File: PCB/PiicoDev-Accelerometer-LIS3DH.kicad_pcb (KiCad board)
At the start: 2 copper layers, 25.4 x 25.4 mm, 37 parts, among them J1 , J2 , J3 Conn_PiicoDev_header_01x04_Ma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, J4 INT, SW1 ASW, U1 LIS3DH

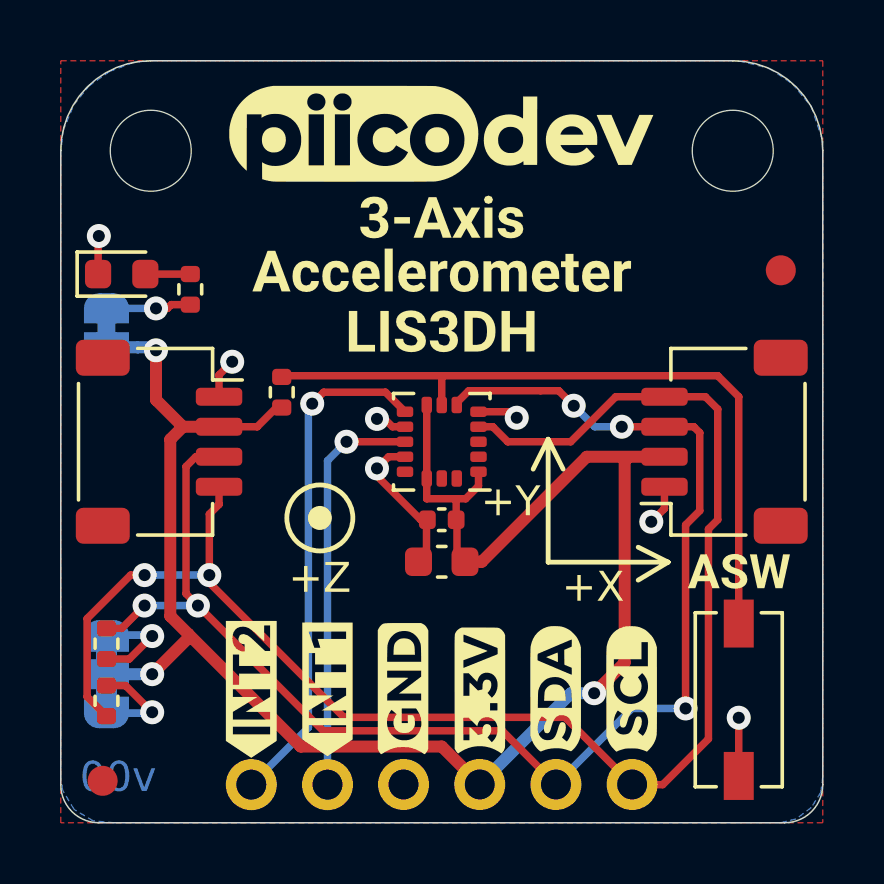
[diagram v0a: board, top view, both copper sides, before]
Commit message: add documents and link CAD
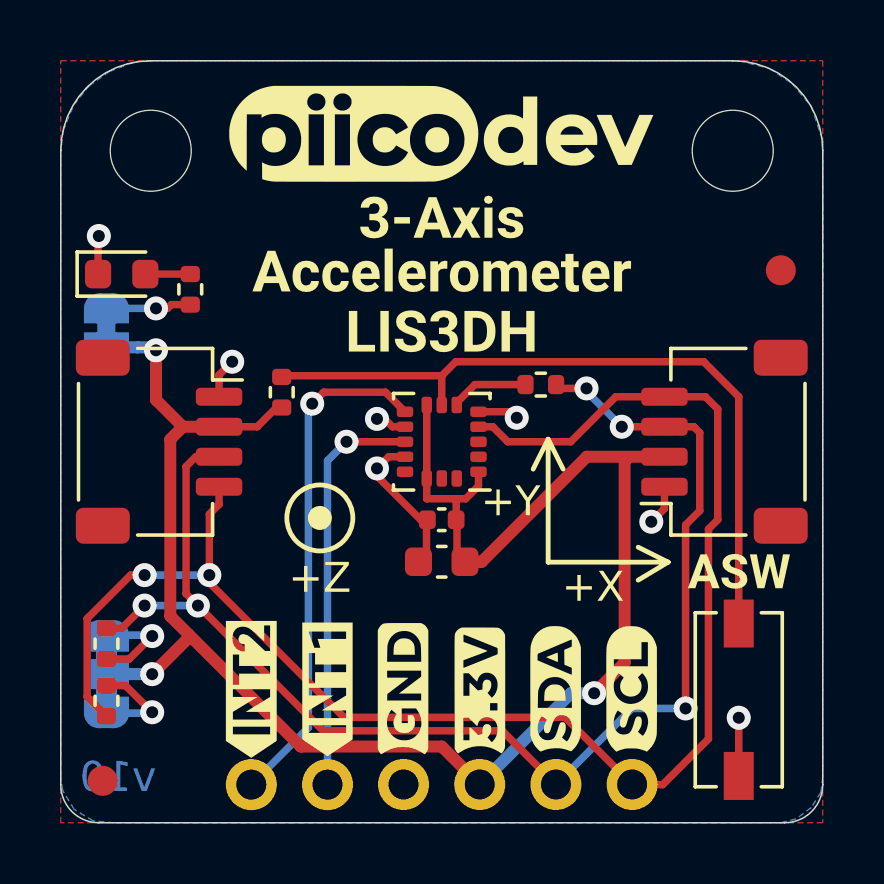
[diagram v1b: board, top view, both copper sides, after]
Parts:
- added R5: 120R, Resistor_SMD:R_0402_1005Metric, F.Cu at (100.6, 99.4)
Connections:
- U1 pad 6: /SDA -> Net-(U1-Pad6)
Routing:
- net /SDA: track 47.5 -> 44.1 mm
- net Net-(U1-Pad6): track 0.00 -> 2.62 mm
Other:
- board text added: "v10"
- board text removed: "v00"
